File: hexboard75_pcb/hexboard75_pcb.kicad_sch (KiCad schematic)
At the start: 30 parts, among them J1 USB_C_Receptacle_USB2.0_14P, SW1 SW_Push, U1 RP2040, U2 NCP1117-3.3_SOT223, U3 W25Q128JVS, Y1 12 MHz

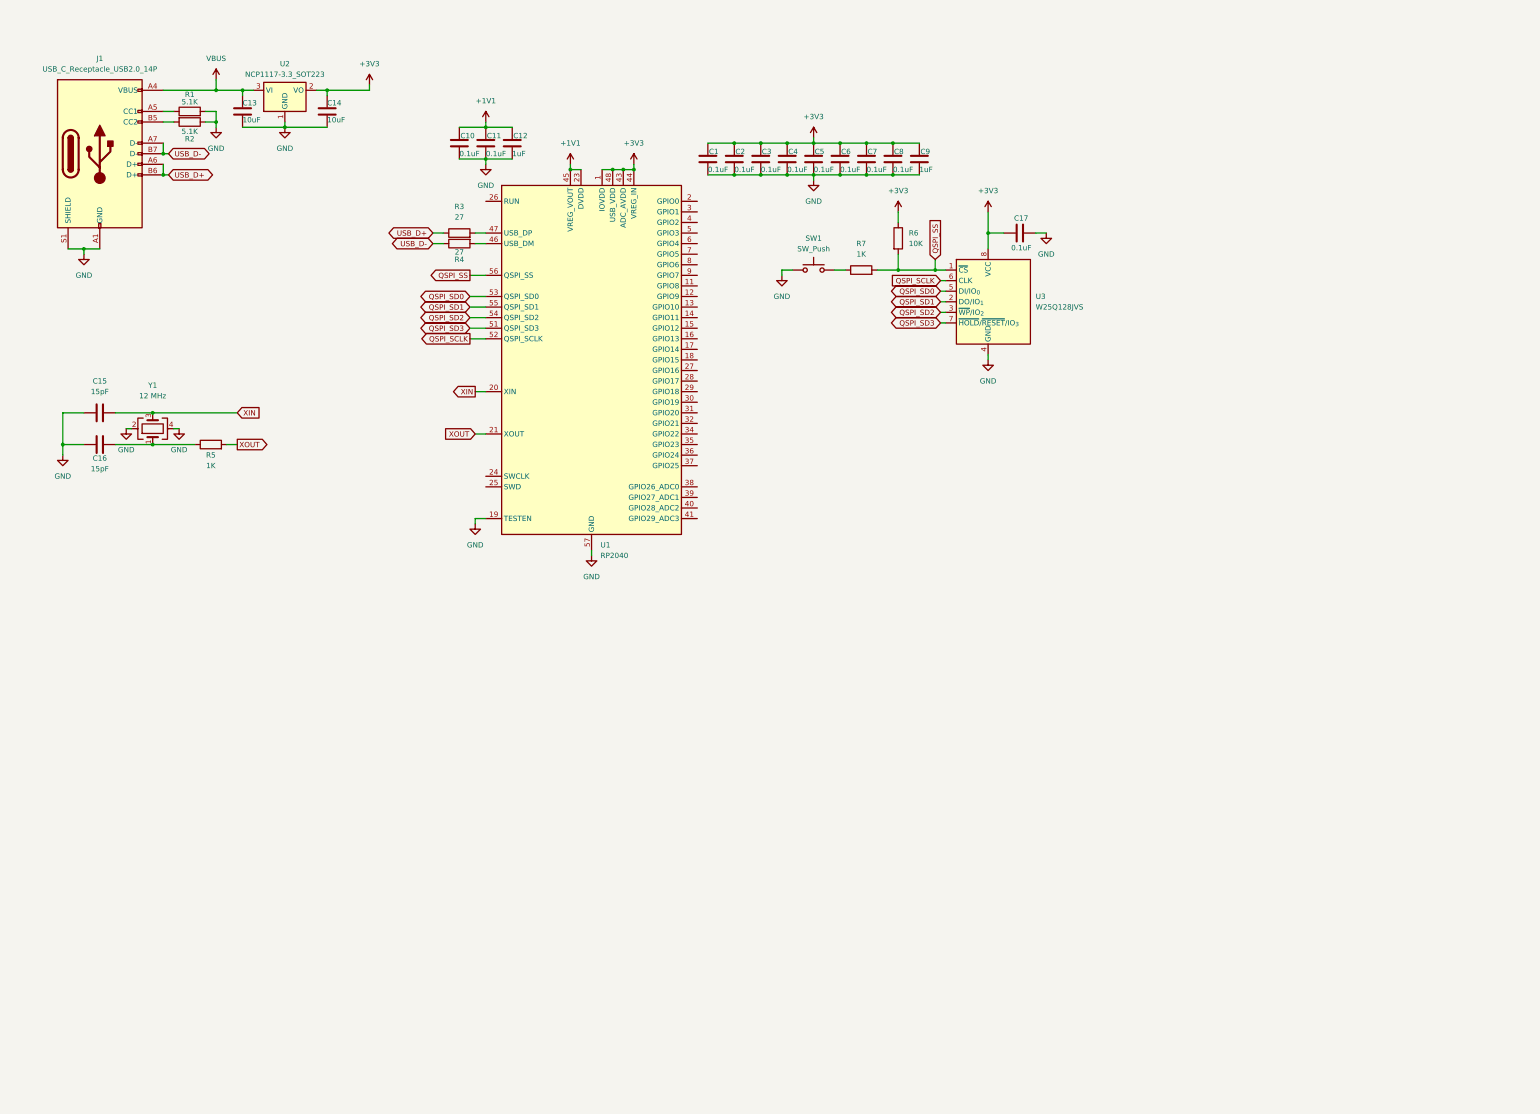
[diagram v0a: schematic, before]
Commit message: finalized schematic
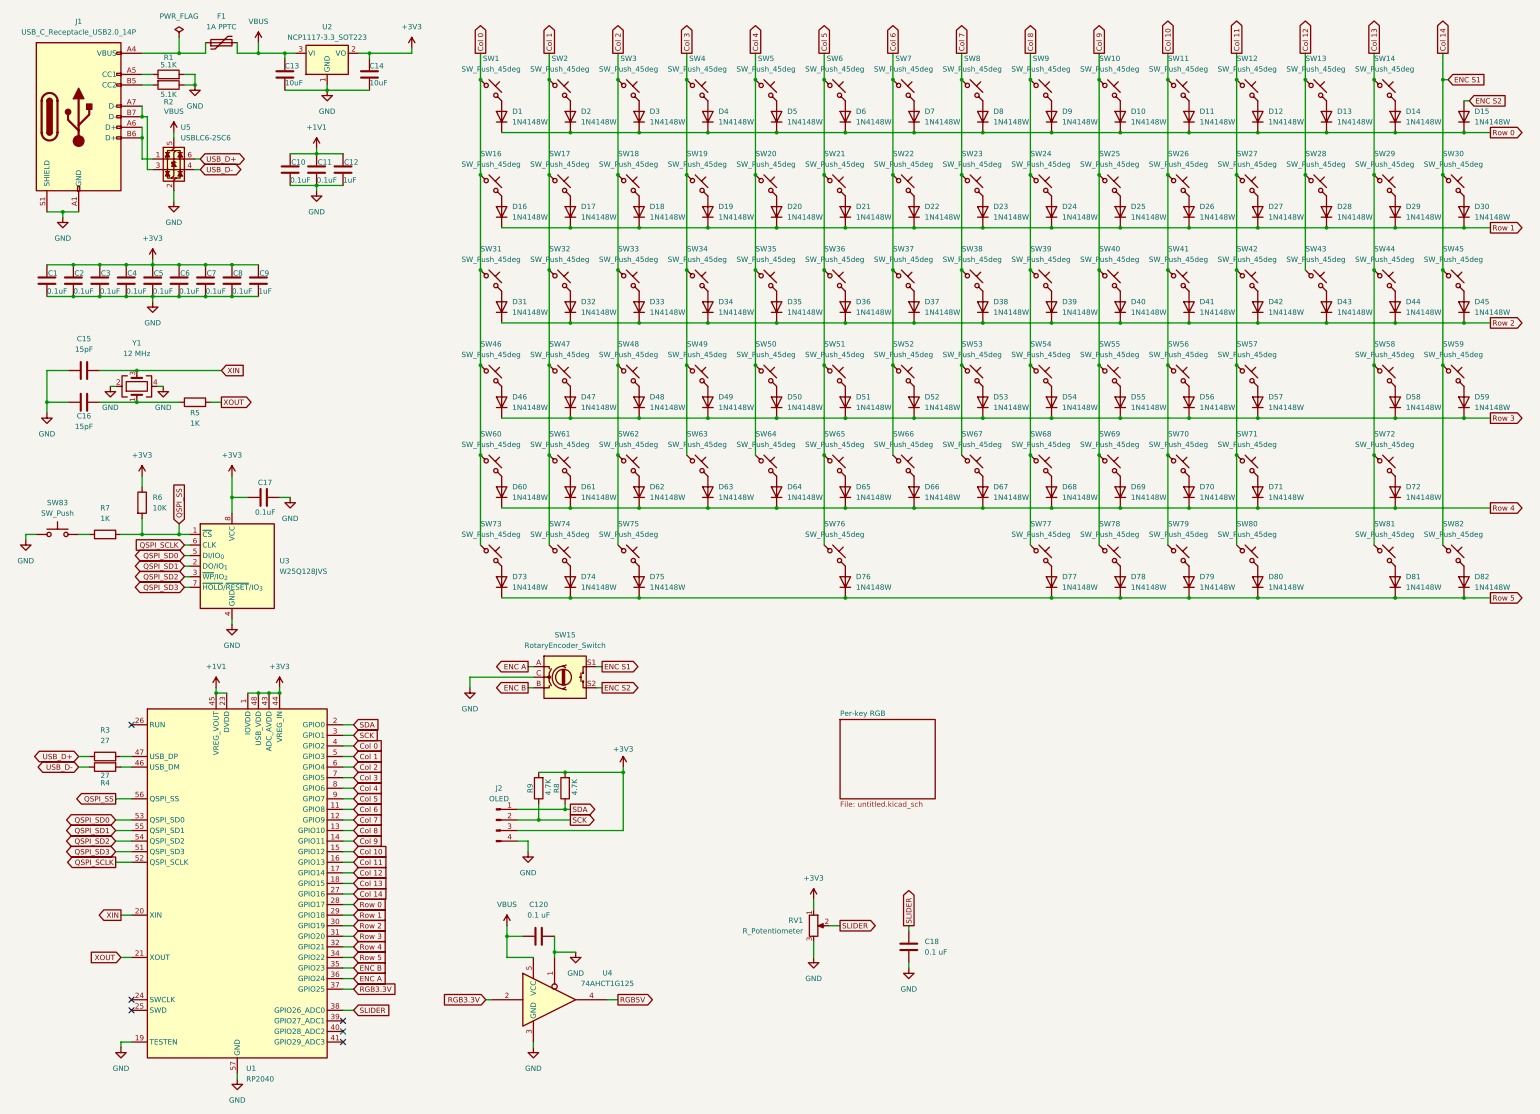
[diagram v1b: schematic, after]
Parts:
- removed SW1: SW_Push, symbol Switch:SW_Push
- added C120, C18: 0.1 uF, symbol Device:C
- added D1, D10, D11, D12, D13, D14, D15, D16, D17, D18, D19, D2, D20, D21, D22, D23, D24, D25, D26, D27, D28, D29, D3, D30, D31, D32, D33, D34, D35, D36, D37, D38, D39, D4, D40, D41, D42, D43, D44, D45, D46, D47, D48, D49, D5, D50, D51, D52, D53, D54, D55, D56, D57, D58, D59, D6, D60, D61, D62, D63, D64, D65, D66, D67, D68, D69, D7, D70, D71, D72, D73, D74, D75, D76, D77, D78, D79, D8, D80, D81, D82, D9: 1N4148W, Diode_SMD:D_SOD-123, symbol Diode:1N4148W
- added F1: 1A PPTC, symbol Device:Polyfuse
- added J2: OLED, Connector_PinHeader_2.54mm:PinHeader_1x04_P2.54mm_Vertical, symbol Connector:Conn_01x04_Pin
- added R8, R9: 4.7K, symbol Device:R
- added RV1: R_Potentiometer, Potentiometer_THT:Potentiometer_Bourns_3296W_Vertical, symbol Device:R_Potentiometer
- added SW1, SW10, SW11, SW12, SW13, SW14, SW16, SW17, SW18, SW19, SW2, SW20, SW21, SW22, SW23, SW24, SW25, SW26, SW27, SW28, SW29, SW3, SW30, SW31, SW32, SW33, SW34, SW35, SW36, SW37, SW38, SW39, SW4, SW40, SW41, SW42, SW43, SW44, SW45, SW46, SW47, SW48, SW49, SW5, SW50, SW51, SW52, SW53, SW54, SW55, SW56, SW57, SW58, SW59, SW6, SW60, SW61, SW62, SW63, SW64, SW65, SW66, SW67, SW68, SW69, SW7, SW70, SW71, SW72, SW73, SW74, SW75, SW76, SW77, SW78, SW79, SW8, SW80, SW81, SW82, SW9: SW_Push_45deg, symbol Switch:SW_Push_45deg
- added SW15: RotaryEncoder_Switch, symbol Device:RotaryEncoder_Switch
- added SW83: SW_Push, symbol Switch:SW_Push
- added U4: 74AHCT1G125, Package_TO_SOT_SMD:SOT-23-5, symbol 74xGxx:74AHCT1G125
- added U5: USBLC6-2SC6, Package_TO_SOT_SMD:SOT-23-6, symbol Power_Protection:USBLC6-2SC6
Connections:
- net +3V3: now also J2.3 (Pin_3), R8.2, R9.2, RV1.1
- net GND: now also C120.2, C18.2, J2.4 (Pin_4), RV1.3, SW15.C, SW83.1, U4.1, U4.3 (GND), U5.2 (GND)
- net USB_D+: now also U5.6 (I/O1); no longer J1.A6 (D+), J1.B6 (D+)
- net USB_D-: now also U5.4 (I/O2); no longer J1.A7 (D-), J1.B7 (D-)
- net VBUS: now also C120.1, F1.2, U4.5 (VCC), U5.5 (VBUS); no longer J1.A4 (VBUS), J1.A9 (VBUS), J1.B4 (VBUS), J1.B9 (VBUS)
- net at R7.1: now also SW83.2
- net Col 6: now reaches U1.11 (GPIO8)
- net Col 6: now also SW22.1, SW37.1, SW52.1, SW66.1, SW7.1
- net Col 7: now reaches U1.12 (GPIO9)
- net Col 7: now also SW23.1, SW38.1, SW53.1, SW67.1, SW8.1
- net Col 8: now reaches U1.13 (GPIO10)
- net Col 8: now also SW24.1, SW39.1, SW54.1, SW68.1, SW77.1, SW9.1
- net Col 9: now reaches U1.14 (GPIO11)
- net Col 9: now also SW10.1, SW25.1, SW40.1, SW55.1, SW69.1, SW78.1
- net Col 10: now reaches U1.15 (GPIO12)
- net Col 10: now also SW11.1, SW26.1, SW41.1, SW56.1, SW70.1, SW79.1
- net Col 11: now reaches U1.16 (GPIO13)
- net Col 11: now also SW12.1, SW27.1, SW42.1, SW57.1, SW71.1, SW80.1
- net Col 12: now reaches U1.17 (GPIO14)
- net Col 12: now also SW13.1, SW28.1, SW43.1
- net Col 13: now reaches U1.18 (GPIO15)
- net Col 13: now also SW14.1, SW29.1, SW44.1, SW58.1, SW72.1, SW81.1
- net SDA: now reaches U1.2 (GPIO0)
- net SDA: now also J2.1 (Pin_1), R8.1
- net Col 14: now reaches U1.27 (GPIO16)
- net Col 14: now also SW15.S1, SW30.1, SW45.1, SW59.1, SW82.1
- net Row 0: now reaches U1.28 (GPIO17)
- net Row 0: now also D1.1 (K), D10.1 (K), D11.1 (K), D12.1 (K), D13.1 (K), D14.1 (K), D15.1 (K), D2.1 (K), D3.1 (K), D4.1 (K), D5.1 (K), D6.1 (K), D7.1 (K), D8.1 (K), D9.1 (K)
- net Row 1: now reaches U1.29 (GPIO18)
- net Row 1: now also D16.1 (K), D17.1 (K), D18.1 (K), D19.1 (K), D20.1 (K), D21.1 (K), D22.1 (K), D23.1 (K), D24.1 (K), D25.1 (K), D26.1 (K), D27.1 (K), D28.1 (K), D29.1 (K), D30.1 (K)
- net SCK: now reaches U1.3 (GPIO1)
- net SCK: now also J2.2 (Pin_2), R9.1
- net Row 2: now reaches U1.30 (GPIO19)
- net Row 2: now also D31.1 (K), D32.1 (K), D33.1 (K), D34.1 (K), D35.1 (K), D36.1 (K), D37.1 (K), D38.1 (K), D39.1 (K), D40.1 (K), D41.1 (K), D42.1 (K), D43.1 (K), D44.1 (K), D45.1 (K)
- net Row 3: now reaches U1.31 (GPIO20)
- net Row 3: now also D46.1 (K), D47.1 (K), D48.1 (K), D49.1 (K), D50.1 (K), D51.1 (K), D52.1 (K), D53.1 (K), D54.1 (K), D55.1 (K), D56.1 (K), D57.1 (K), D58.1 (K), D59.1 (K)
- net Row 4: now reaches U1.32 (GPIO21)
- net Row 4: now also D60.1 (K), D61.1 (K), D62.1 (K), D63.1 (K), D64.1 (K), D65.1 (K), D66.1 (K), D67.1 (K), D68.1 (K), D69.1 (K), D70.1 (K), D71.1 (K), D72.1 (K)
- net Row 5: now reaches U1.34 (GPIO22)
- net Row 5: now also D73.1 (K), D74.1 (K), D75.1 (K), D76.1 (K), D77.1 (K), D78.1 (K), D79.1 (K), D80.1 (K), D81.1 (K), D82.1 (K)
- net ENC B: now reaches U1.35 (GPIO23)
- net ENC B: now also SW15.B
- net ENC A: now reaches U1.36 (GPIO24)
- net ENC A: now also SW15.A
- net RGB3.3V: now reaches U1.37 (GPIO25)
- net RGB3.3V: now also U4.2
- net SLIDER: now reaches U1.38 (GPIO26_ADC0)
- net SLIDER: now also C18.1, RV1.2
- net Col 0: now reaches U1.4 (GPIO2)
- net Col 0: now also SW1.1, SW16.1, SW31.1, SW46.1, SW60.1, SW73.1
- net Col 1: now reaches U1.5 (GPIO3)
- net Col 1: now also SW17.1, SW2.1, SW32.1, SW47.1, SW61.1, SW74.1
- net Col 2: now reaches U1.6 (GPIO4)
- net Col 2: now also SW18.1, SW3.1, SW33.1, SW48.1, SW62.1, SW75.1
- net Col 3: now reaches U1.7 (GPIO5)
- net Col 3: now also SW19.1, SW34.1, SW4.1, SW49.1, SW63.1
- net Col 4: now reaches U1.8 (GPIO6)
- net Col 4: now also SW20.1, SW35.1, SW5.1, SW50.1, SW64.1
- net Col 5: now reaches U1.9 (GPIO7)
- net Col 5: now also SW21.1, SW36.1, SW51.1, SW6.1, SW65.1, SW76.1
- new net: D80.2 (A), SW80.2
- new net: D27.2 (A), SW27.2
- new net: D77.2 (A), SW77.2
- new net: D47.2 (A), SW47.2
- new net: D25.2 (A), SW25.2
- new net: D30.2 (A), SW30.2
- new net: D10.2 (A), SW10.2
- new net: D16.2 (A), SW16.2
- new net: D65.2 (A), SW65.2
- new net: D1.2 (A), SW1.2
- new net: D37.2 (A), SW37.2
- new net: D78.2 (A), SW78.2
- new net: D20.2 (A), SW20.2
- new net: D34.2 (A), SW34.2
- new net: D43.2 (A), SW43.2
- new net: D28.2 (A), SW28.2
- new net: D66.2 (A), SW66.2
- new net: D70.2 (A), SW70.2
- new net: D5.2 (A), SW5.2
- new net: D79.2 (A), SW79.2
- new net: D63.2 (A), SW63.2
- new net: D57.2 (A), SW57.2
- new net: D36.2 (A), SW36.2
- new net: D60.2 (A), SW60.2
- new net: D2.2 (A), SW2.2
- new net: D14.2 (A), SW14.2
- new net: D11.2 (A), SW11.2
- new net: D24.2 (A), SW24.2
- new net: D53.2 (A), SW53.2
- new net: D13.2 (A), SW13.2
- new net: D74.2 (A), SW74.2
- new net: D55.2 (A), SW55.2
- new net: D67.2 (A), SW67.2
- new net: D6.2 (A), SW6.2
- new net: D51.2 (A), SW51.2
- new net: D59.2 (A), SW59.2
- new net: D23.2 (A), SW23.2
- new net: D75.2 (A), SW75.2
- new net: D38.2 (A), SW38.2
- new net: J1.A6 (D+), J1.B6 (D+), U5.1 (I/O1)
- new net: J1.A7 (D-), J1.B7 (D-), U5.3 (I/O2)
- new net: D48.2 (A), SW48.2
- new net: D62.2 (A), SW62.2
- new net: D69.2 (A), SW69.2
- new net: D40.2 (A), SW40.2
- new net: D76.2 (A), SW76.2
- new net: D8.2 (A), SW8.2
- new net: D58.2 (A), SW58.2
- new net: D35.2 (A), SW35.2
- new net: D61.2 (A), SW61.2
- new net: D41.2 (A), SW41.2
- new net: D39.2 (A), SW39.2
- new net: D31.2 (A), SW31.2
- new net: D56.2 (A), SW56.2
- new net: D73.2 (A), SW73.2
- new net: F1.1, J1.A4 (VBUS), J1.A9 (VBUS), J1.B4 (VBUS), J1.B9 (VBUS)
- new net: D29.2 (A), SW29.2
- new net: D68.2 (A), SW68.2
- new net: D71.2 (A), SW71.2
- new net: D49.2 (A), SW49.2
- new net: D72.2 (A), SW72.2
- new net: D22.2 (A), SW22.2
- new net: D19.2 (A), SW19.2
- new net: D18.2 (A), SW18.2
- new net: D32.2 (A), SW32.2
- new net: D54.2 (A), SW54.2
- new net: D44.2 (A), SW44.2
- new net: D26.2 (A), SW26.2
- new net: D45.2 (A), SW45.2
- new net: D7.2 (A), SW7.2
- new net: D21.2 (A), SW21.2
- new net: D42.2 (A), SW42.2
- new net: D4.2 (A), SW4.2
- new net: D50.2 (A), SW50.2
- new net: D82.2 (A), SW82.2
- new net: D64.2 (A), SW64.2
- new net: D9.2 (A), SW9.2
- new net: D52.2 (A), SW52.2
- new net: D46.2 (A), SW46.2
- new net: D17.2 (A), SW17.2
- new net: D33.2 (A), SW33.2
- new net: D3.2 (A), SW3.2
- new net: D81.2 (A), SW81.2
- new net: D12.2 (A), SW12.2
- new net ENC S2: D15.2 (A), SW15.S2
- new net RGB5V: U4.4
- no-connect marks 0 -> 6
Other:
- added sheet Per-key RGB (untitled.kicad_sch)
- moved on the sheet: C1, C10, C11, C12, C13, C14, C15, C16, C17, C2, C3, C4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
